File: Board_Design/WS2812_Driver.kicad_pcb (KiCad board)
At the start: 2 copper layers, 27.5 x 24.5 mm, 23 parts, among them J1 5Vin, J10 PogoPin, J11 PogoPin, J12 PogoPin, J2 GNDin, J3 5Vout, J4 DOUT, J5 GNDout, J6 INPUT, J7 PogoPin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

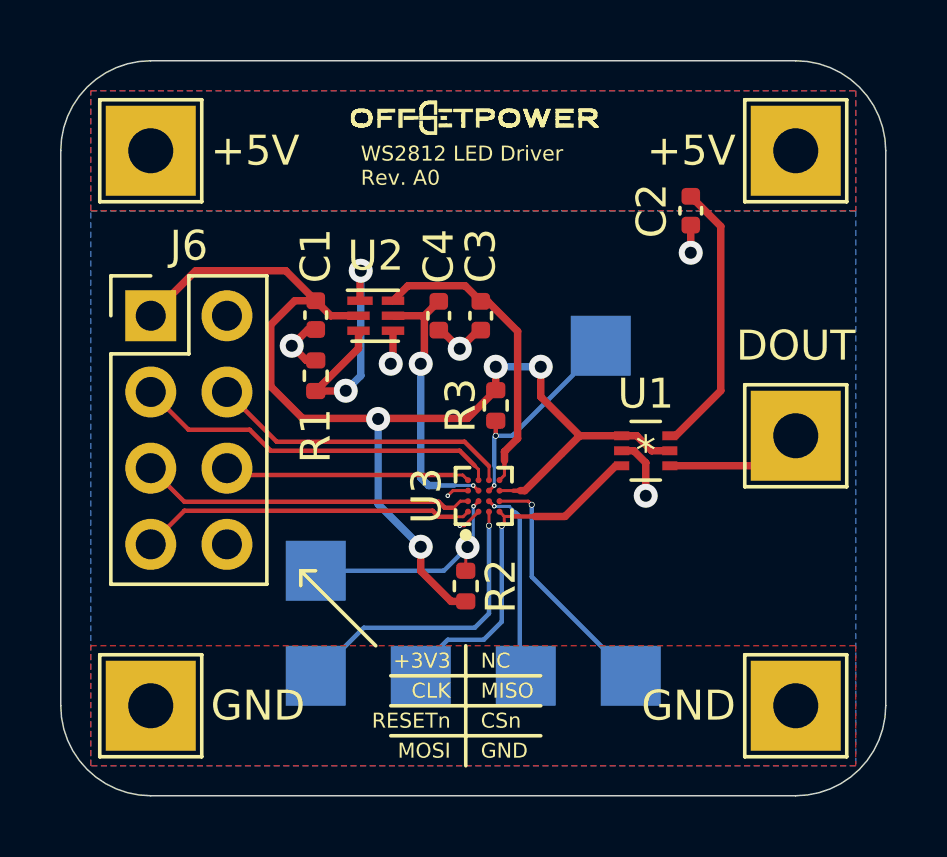
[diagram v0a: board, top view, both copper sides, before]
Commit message: Updated for DFR
Updated design for more design-for-manufacturability.
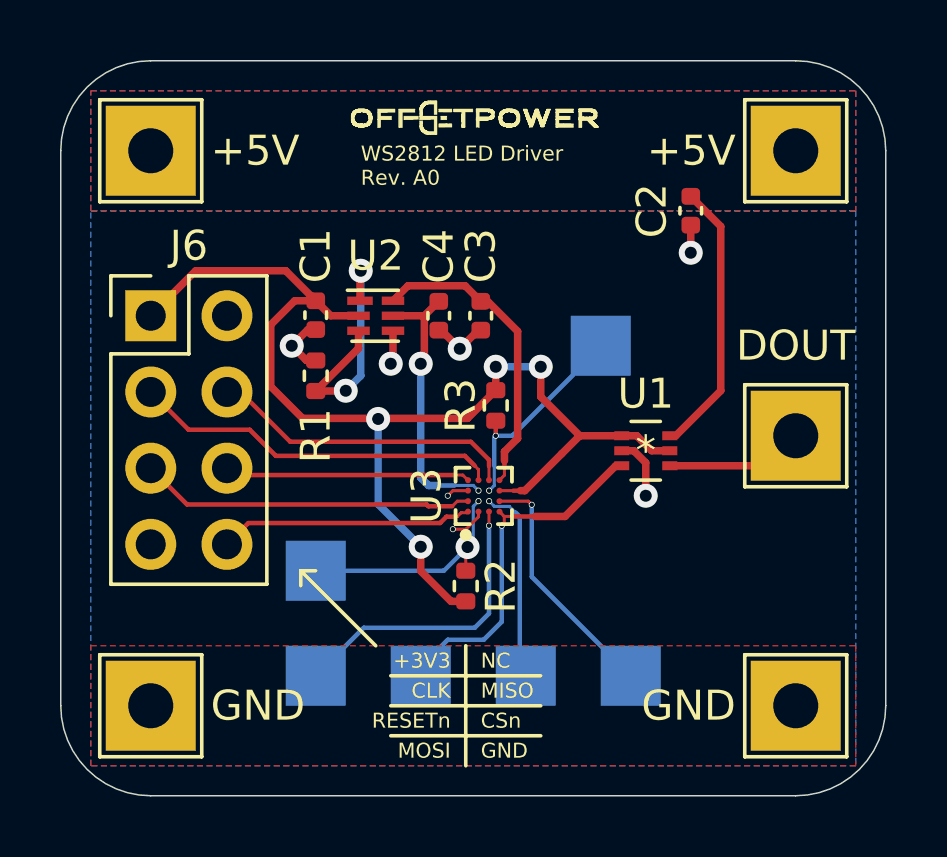
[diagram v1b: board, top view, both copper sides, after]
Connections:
- J6 pad 7: SPI_MOSI -> GND
- J6 pad 8: GND -> SPI_MOSI
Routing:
- net SPI_MOSI: track 11.2 -> 8.49 mm
